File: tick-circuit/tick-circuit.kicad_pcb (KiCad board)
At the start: 2 copper layers, 45.7 x 33 mm, 14 parts, among them J1 Power, J2 50/60Hz, U1 74HCT4060, U2 74HCT73, X1 3.93216 MHz

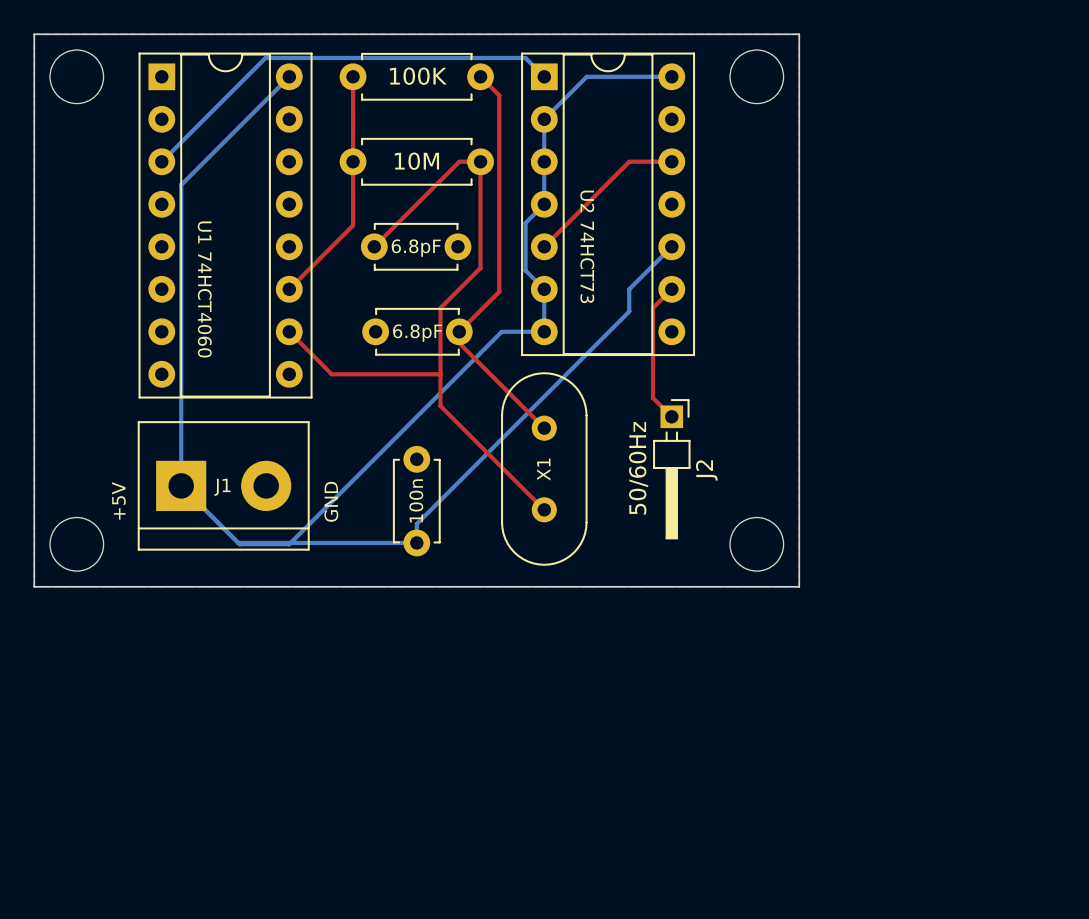
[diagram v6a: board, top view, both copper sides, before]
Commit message: Tick Circuit v2, an altered layout of the board to fit the electrical paths better
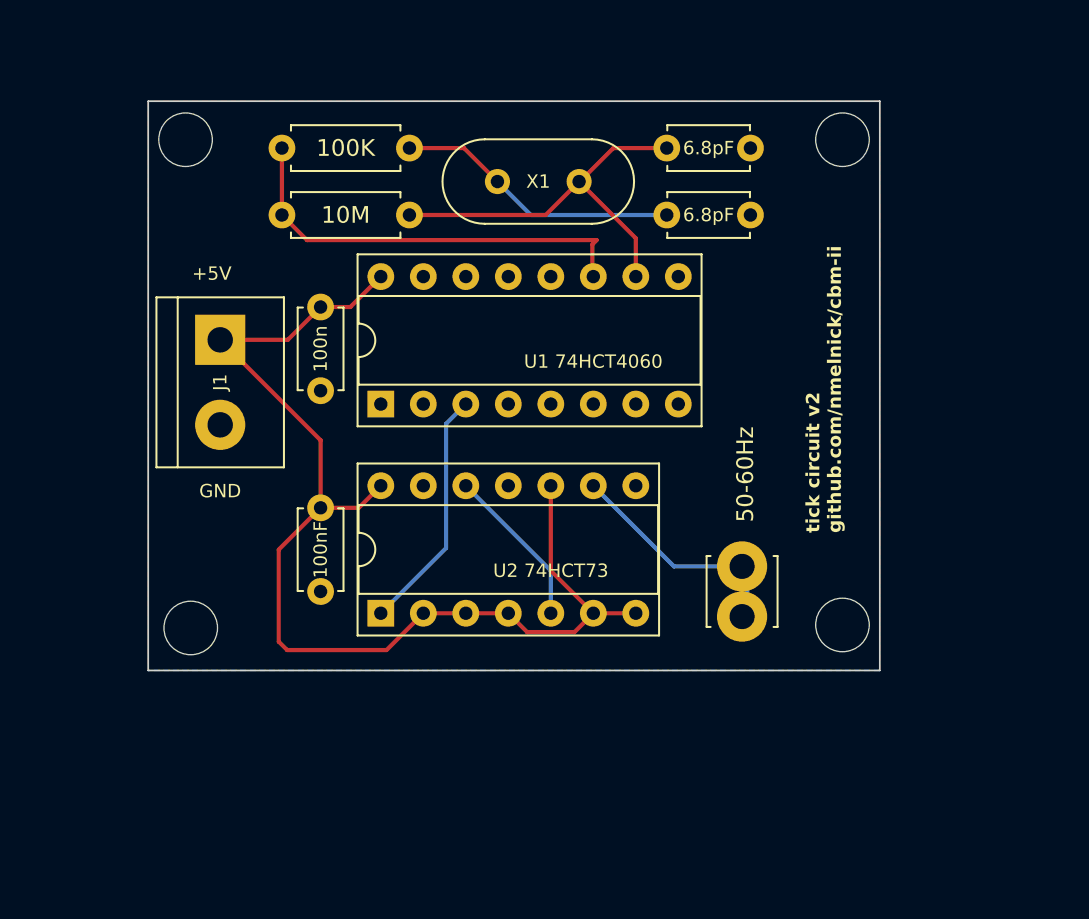
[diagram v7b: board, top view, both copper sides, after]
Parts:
- added C4: 100nF, Capacitor_THT:C_Disc_D4.7mm_W2.5mm_P5.00mm, F.Cu at (29.8, 41.0)
- 50-60Hz: renamed from J2; value 50/60Hz -> 50/60Hz; footprint Connector_PinHeader_2.00mm:PinHeader_1x01_P2.00mm_Horizontal -> TerminalBlock_MetzConnect:TerminalBlock_MetzConnect_360272_1x01_Horizontal_ScrewM2.6
- moved U2 33.5 mm to (33.4, 47.3), turned to 90 degrees
- moved U1 23.5 mm to (33.4, 34.8), turned to 90 degrees
- moved X1 19.7 mm to (45.3, 21.5), turned to 180 degrees
- moved C1 18.4 mm to (50.5, 19.5)
- moved C3 15.2 mm to (29.8, 29.0), turned to -90 degrees
- moved C2 14.2 mm to (50.5, 23.5), turned to 0 degrees
- moved 50-60Hz 9.88 mm to (55.0, 44.5)
- moved J1 9.04 mm to (23.8, 31.0), turned to -90 degrees
- moved REF** 8.45 mm to (22.1, 48.2)
- moved REF** 7.51 mm to (21.7, 19.0)
- moved REF** 7.03 mm to (61.0, 48.0)
- moved REF** 6.35 mm to (61.0, 19.0)
- moved R2 6.02 mm to (27.5, 19.5)
- moved R1 5.31 mm to (35.1, 23.5)
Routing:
- net +5V: track 117.3 -> 69.1 mm
- net Net-(U1-RTC): track 43.4 -> 24.1 mm
- net Net-(U1-RS): track 14.1 -> 25.7 mm
- net Net-(U1-Q13): track 25.9 -> 14.6 mm
- net Net-(C2-Pad1): track 24.6 -> 17.0 mm
- net Net-(J2-Pin_1): track 8.55 -> 13.9 mm
- net GND: track 0.59 -> 0.00 mm
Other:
- board size 45.7 x 33 mm -> 43.7 x 34 mm
- board text added: "tick circuit v2 github.com/nmelnick/cbm-ii"
- board text removed: "tick circuit github.com/nmelnick/cbm-ii"

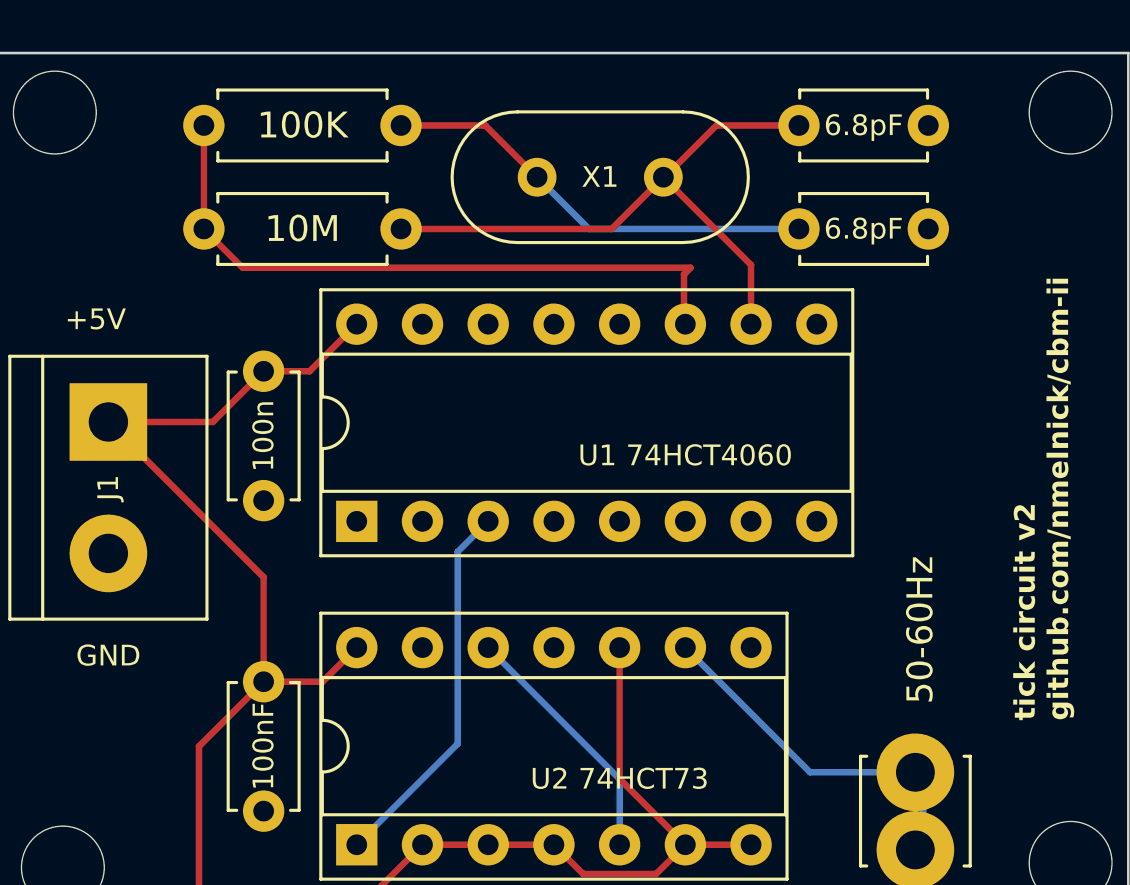
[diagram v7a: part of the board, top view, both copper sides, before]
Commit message: Update resistor footprint to hold a larger one, update README to show test success
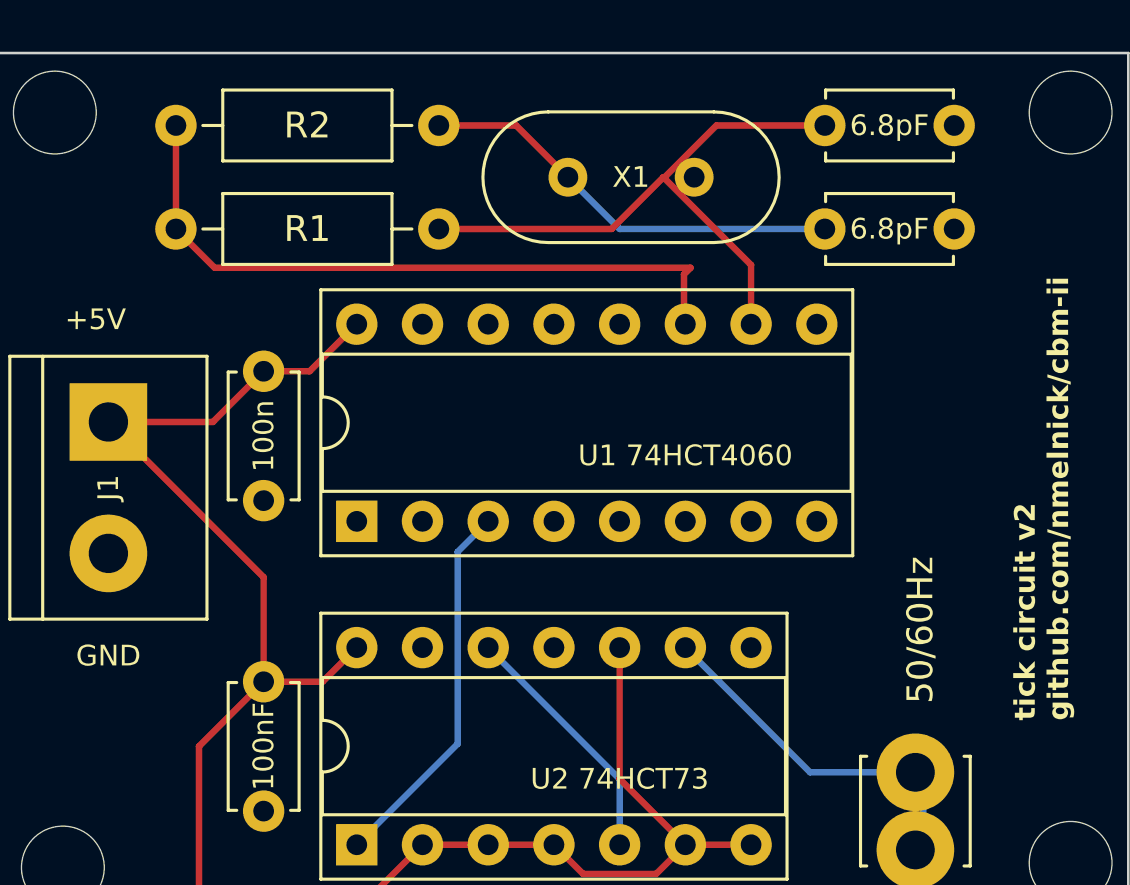
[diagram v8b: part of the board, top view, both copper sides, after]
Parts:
- R1, R2: footprint Resistor_THT:R_Axial_DIN0207_L6.3mm_D2.5mm_P7.62mm_Horizontal -> Resistor_THT:R_Axial_DIN0207_L6.3mm_D2.5mm_P10.16mm_Horizontal
- moved R1 1.46 mm to (36.6, 23.5)
- moved X1 1.19 mm to (46.5, 21.5)
- moved R2 1.08 mm to (26.4, 19.5)
- moved C1 1.00 mm to (51.5, 19.5)
- moved C2 1.00 mm to (51.5, 23.5)
- renumbered 50-60Hz to 50/60Hz
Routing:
- net Net-(U1-RS): track 25.7 -> 26.8 mm
